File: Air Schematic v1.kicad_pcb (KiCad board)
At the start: 2 copper layers, 15 parts

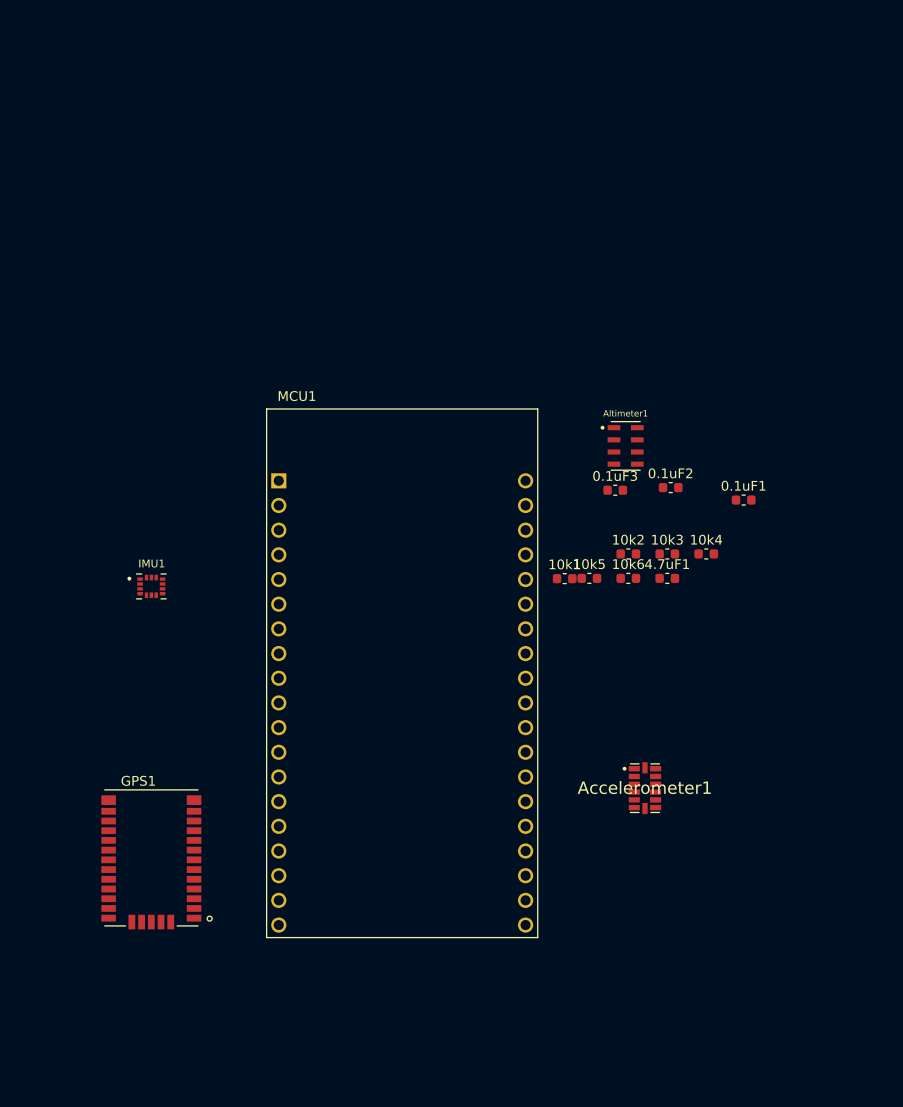
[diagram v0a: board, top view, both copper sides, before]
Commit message: Added footprints, initial pcb layouts
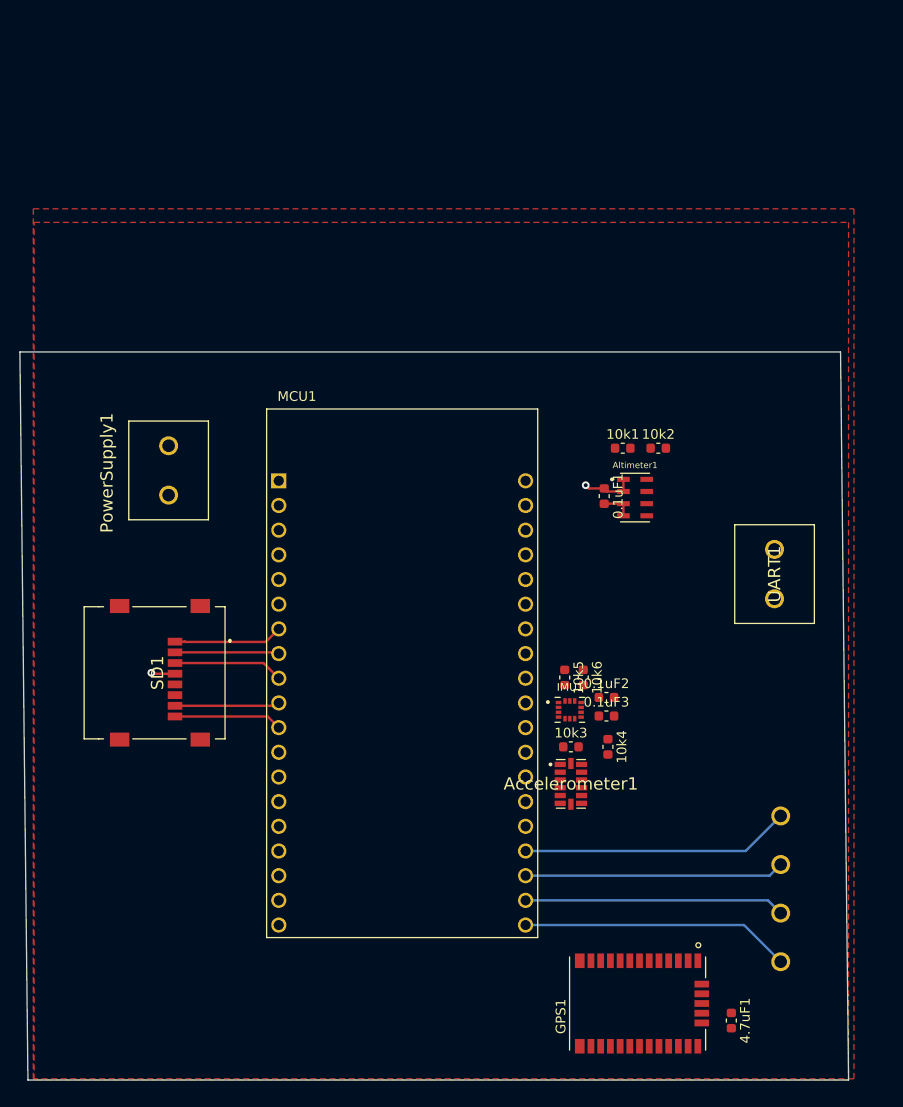
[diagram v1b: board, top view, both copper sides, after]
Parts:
- added PowerSupply1: TB006-508-02BE, SamacSys_Parts:TB00650802BE, F.Cu at (56.4, 57.9)
- added SD1: 47219-2001, SamacSys_Parts:472192001, F.Cu at (55.2, 76.2)
- added SPI1: TB001-500-04BE, SamacSys_Parts:TB00150004BE, B.Cu at (119.4, 90.9)
- added UART1: TB006-508-02BE, SamacSys_Parts:TB00650802BE, F.Cu at (118.7, 63.5)
- moved GPS1 52.2 mm to (104.7, 110.2), turned to 90 degrees
- moved 4.7uF1 46.0 mm to (114.3, 112.0), turned to 270 degrees
- moved IMU1 44.9 mm to (97.7, 80.0)
- moved 0.1uF3 23.3 mm to (101.4, 80.6)
- moved 0.1uF2 22.6 mm to (101.4, 78.7)
- moved 10k4 22.3 mm to (101.6, 83.8), turned to 270 degrees
- moved 10k3 22.2 mm to (97.8, 83.8)
- moved 10k1 14.7 mm to (103.1, 53.1)
- moved 0.1uF1 14.4 mm to (101.2, 58.0), turned to 270 degrees
- moved 10k2 11.3 mm to (106.8, 53.1)
- moved 10k6 11.2 mm to (99.1, 76.7), turned to 270 degrees
- moved 10k5 10.5 mm to (97.2, 76.7), turned to 270 degrees
- moved Accelerometer1 7.63 mm to (97.8, 87.6)
- moved Altimeter1 5.40 mm to (104.4, 58.2)
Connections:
- Accelerometer1 pad 9: Net-(Accelerometer1-Pad9) -> ACCEL_READY
- IMU1 pad 4: Net-(IMU1-Pad4) -> IMU_READY
- MCU1 pad 10: Net-(MCU1-Pad10) -> Dat0
- MCU1 pad 11: Net-(MCU1-Pad11) -> Dat1
- MCU1 pad 29: Net-(MCU1-Pad29) -> GPS_READY
- MCU1 pad 30: Net-(MCU1-Pad30) -> IMU_READY
- MCU1 pad 31: Net-(MCU1-Pad31) -> ACCEL_READY
- MCU1 pad 7: Net-(MCU1-Pad7) -> Dat2
- MCU1 pad 8: Net-(MCU1-Pad8) -> Dat3
- MCU1 pad 9: Net-(MCU1-Pad9) -> CMD
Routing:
- net CLK: track 0.00 -> 27.8 mm
- net CS: track 0.00 -> 27.7 mm
- net MOSI: track 0.00 -> 26.8 mm
- net MISO: track 0.00 -> 26.7 mm
- net CMD: track 0.00 -> 11.3 mm
- net Dat2: track 0.00 -> 11.2 mm
- net Dat1: track 0.00 -> 11.2 mm
- net Dat0: track 0.00 -> 10.8 mm
- net Dat3: track 0.00 -> 10.7 mm
- net +3V3: track 0.00 -> 7.87 mm, vias 0 -> 2
- net GND: track 0.00 -> 3.23 mm
- added copper zone on F.Cu, net +3V3
- added copper zone on F.Cu, net GND
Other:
- board outline added: 85.3 x 74.9 mm

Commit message: Switched out altimeter and IMU
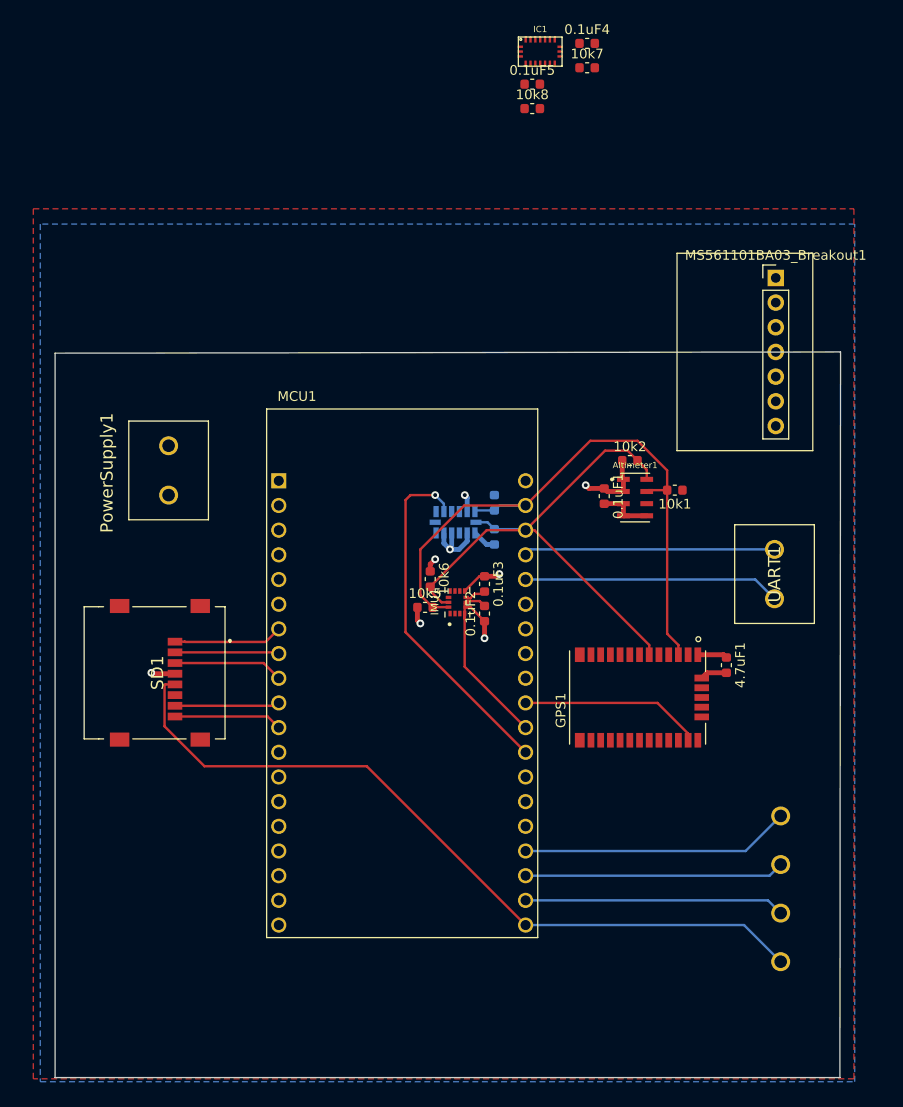
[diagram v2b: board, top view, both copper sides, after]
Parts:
- added 0.1uF4: C, Capacitor_SMD:C_0603_1608Metric, F.Cu at (99.5, 11.4)
- added 0.1uF5: C, Capacitor_SMD:C_0603_1608Metric, F.Cu at (93.8, 15.6)
- added 10k7: R, Resistor_SMD:R_0603_1608Metric, F.Cu at (99.5, 13.9)
- added 10k8: R, Resistor_SMD:R_0603_1608Metric, F.Cu at (93.8, 18.1)
- added IC1: BMX055, BMX055:BMX055, F.Cu at (94.6, 12.3)
- added MS561101BA03_Breakout1: Altimeter, MS561101BA03-50:Inexact_Altimeter_Breakout, F.Cu at (118.9, 35.6)
- 10k3, 10k4, Accelerometer1: moved to B.Cu
- moved 4.7uF1 36.6 mm to (113.8, 75.4)
- moved GPS1 31.5 mm to (104.7, 78.7)
- moved Accelerometer1 29.4 mm to (85.9, 60.7), turned to 90 degrees
- moved 10k4 27.7 mm to (89.9, 58.7)
- moved 10k3 23.0 mm to (89.9, 62.2), turned to 90 degrees
- moved 10k6 18.7 mm to (83.3, 66.5)
- moved 0.1uF3 18.5 mm to (88.9, 67.1), turned to 270 degrees
- moved 10k5 16.1 mm to (82.8, 69.5), turned to 0 degrees
- moved IMU1 16.0 mm to (86.1, 68.9), turned to 90 degrees
- moved 0.1uF2 15.2 mm to (88.9, 70.1), turned to 90 degrees
- moved 10k1 6.88 mm to (108.5, 57.4), turned to 180 degrees
- moved 10k2 3.19 mm to (103.9, 54.4)
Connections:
- 4.7uF1 pad 1: +3V3 -> Net-(4.7uF1-Pad1)
- SD1 pad 5: SDIOCLK? -> CLK
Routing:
- net SDA: track 0.00 -> 66.5 mm
- net SCLK: track 0.00 -> 56.8 mm
- net CLK: track 27.8 -> 78.8 mm
- net ACCEL_READY: track 0.00 -> 36.4 mm, vias 0 -> 1
- net RX: track 0.00 -> 26.4 mm
- net TX: track 0.00 -> 25.9 mm
- net +3V3: track 7.87 -> 27.1 mm, vias 2 -> 6
- net GPS_READY: track 0.00 -> 18.7 mm
- net GND: track 3.23 -> 21.2 mm, vias 0 -> 2
- net IMU_READY: track 0.00 -> 15.9 mm
- added copper zone on B.Cu, net +3V3
- removed copper zone on F.Cu, net +3V3
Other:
- board size 85.3 x 74.9 mm -> 80.8 x 74.7 mm
- net class Gnd added: clearance 0.2, trace_width 0.5, via_dia 0.8, via_drill 0.4
- net class Power added: clearance 0.2, trace_width 0.5, via_dia 0.8, via_drill 0.4

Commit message: Updated schematic, pcb, a really messy bom
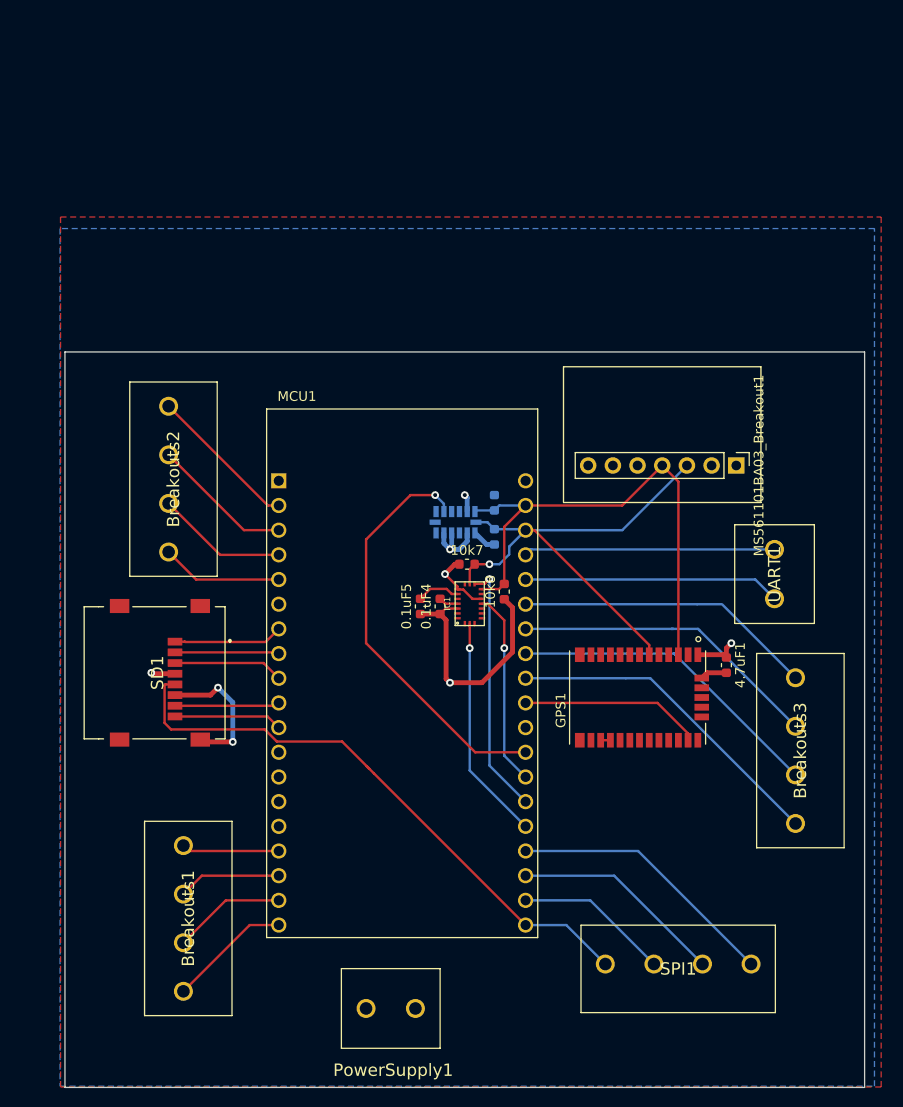
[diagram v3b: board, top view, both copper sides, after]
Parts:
- removed 0.1uF1, 0.1uF2, 0.1uF3: C, Capacitor_SMD:C_0603_1608Metric
- removed 10k1, 10k2, 10k5, 10k6: R, Resistor_SMD:R_0603_1608Metric
- removed Altimeter1: MS561101BA03-50, MS561101BA03-50:SON125P500X300X100-8N
- removed IMU1: BMX160, BMX160:PQFN50P250X300X100-14N
- added Breakouts1: TB001-500-04BE, SamacSys_Parts:TB00150004BE, F.Cu at (57.9, 94.0)
- added Breakouts2: TB001-500-04BE, SamacSys_Parts:TB00150004BE, F.Cu at (56.4, 48.8)
- added Breakouts3: TB001-500-04BE, SamacSys_Parts:TB00150004BE, F.Cu at (120.9, 76.7)
- SPI1: moved to F.Cu
- moved 0.1uF4 59.9 mm to (84.3, 69.4), turned to 90 degrees
- moved PowerSupply1 58.6 mm to (81.8, 110.7), turned to 180 degrees
- moved IC1 57.3 mm to (87.4, 69.1), turned to 90 degrees
- moved 0.1uF5 55.0 mm to (82.3, 69.4), turned to 90 degrees
- moved 10k7 52.6 mm to (87.1, 65.0)
- moved 10k8 49.8 mm to (90.9, 67.8), turned to 90 degrees
- moved MS561101BA03_Breakout1 19.7 mm to (114.8, 54.9), turned to 270 degrees
- moved SPI1 15.5 mm to (116.3, 106.2), turned to 180 degrees
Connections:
- 4.7uF1 pad 1: Net-(4.7uF1-Pad1) -> +3V3
- IC1 pad 10: Net-(IC1-Pad10) -> GYRO_READY
- IC1 pad 14: Net-(IC1-Pad14) -> MAGNET_READY
- IC1 pad 19: Net-(IC1-Pad19) -> ACCEL2_READY
- MCU1 pad 32: Net-(MCU1-Pad32) -> MAGNET_READY
- MCU1 pad 33: Net-(MCU1-Pad33) -> GYRO_READY
- MCU1 pad 34: Net-(MCU1-Pad34) -> ACCEL2_READY
- MS561101BA03_Breakout1 pad 1: (no net) -> +3V3
- MS561101BA03_Breakout1 pad 2: (no net) -> GND
- MS561101BA03_Breakout1 pad 3: (no net) -> SCLK
- MS561101BA03_Breakout1 pad 4: (no net) -> SDA
- MS561101BA03_Breakout1 pad 5: (no net) -> Net-(MS561101BA03_Breakout1-Pad5)
- MS561101BA03_Breakout1 pad 6: (no net) -> Net-(MS561101BA03_Breakout1-Pad6)
- MS561101BA03_Breakout1 pad 7: (no net) -> Net-(MS561101BA03_Breakout1-Pad7)
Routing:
- net Net-(Breakouts3-Pad4): track 0.00 -> 34.0 mm
- net Net-(Breakouts3-Pad3): track 0.00 -> 33.0 mm
- net Net-(Breakouts3-Pad2): track 0.00 -> 32.1 mm
- net Net-(Breakouts3-Pad1): track 0.00 -> 30.8 mm
- net GYRO_READY: track 0.00 -> 26.2 mm, vias 0 -> 1
- net ACCEL2_READY: track 0.00 -> 23.2 mm, vias 0 -> 1
- net MAGNET_READY: track 0.00 -> 20.0 mm, vias 0 -> 1
- net CLK: track 78.8 -> 61.0 mm
- net IMU_READY: track 15.9 -> 0.00 mm
- net Net-(Breakouts2-Pad1): track 0.00 -> 15.6 mm
- net +3V3: track 27.1 -> 41.7 mm, vias 6 -> 4
- net Net-(Breakouts2-Pad2): track 0.00 -> 14.5 mm
- net SDA: track 66.5 -> 52.9 mm
- net Net-(Breakouts2-Pad3): track 0.00 -> 13.5 mm
- net Net-(Breakouts1-Pad4): track 0.00 -> 12.6 mm
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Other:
- board size 80.8 x 74.7 mm -> 82.3 x 75.7 mm
